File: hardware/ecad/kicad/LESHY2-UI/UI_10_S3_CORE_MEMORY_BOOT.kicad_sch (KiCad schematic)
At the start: 0 parts

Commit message: Complete H2.2.2 S3 core schematic
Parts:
- added C1: Murata GRM1555C1H390JA01D, Capacitor_SMD:C_0402_1005Metric, symbol Leshy2:UI10_S3_DETECTOR_INPUT_CAP
- added C2: KEMET C0402C330J5GACTU, Capacitor_SMD:C_0402_1005Metric, symbol Leshy2:UI10_S3_DETECTOR_OUTPUT_CAP
- added C3: TDK C1005X7R1H104K050BB, Capacitor_SMD:C_0402_1005Metric, symbol Leshy2:UI10_S3_DETECTOR_BYPASS
- added C4: TDK C1005X7R1H104K050BB, Capacitor_SMD:C_0402_1005Metric, symbol Leshy2:UI10_S3_SUPPLY_BYPASS
- added C5: TDK C1608X7R1C105K080AC, Capacitor_SMD:C_0603_1608Metric, symbol Leshy2:UI10_S3_RESET_DELAY_CAP
- added J1: GCT RFPC-SMA32-FN-175-A, Leshy2:RFPC-SMA32-FN-175-A, symbol Leshy2:UI10_S3_EXTERNAL_RP_SMA
- added J2: Hirose U.FL-R-SMT-1(10), Connector_Coaxial:U.FL_Hirose_U.FL-R-SMT-1_Vertical, symbol Leshy2:UI10_S3_RF_BOARD_CONNECTOR
- added J3: Samtec FTSH-105-01-L-DV-K-P-TR, Leshy2:FTSH-105-01-L-DV-K-P-TR, symbol Leshy2:UI10_S3_DBG_HEADER
- added R1: Yageo RC0402FR-0749R9L, Resistor_SMD:R_0402_1005Metric, symbol Leshy2:UI10_S3_RF_COUPLER_TERMINATION
- added R10: Yageo RC0402FR-071KL, Resistor_SMD:R_0402_1005Metric, symbol Leshy2:UI10_S3_DBG_RESET_SERIES
- added R11: Yageo RC0402FR-071KL, Resistor_SMD:R_0402_1005Metric, symbol Leshy2:UI10_S3_DBG_BOOT_SERIES
- added R12: Yageo RC0402FR-07470RL, Resistor_SMD:R_0402_1005Metric, symbol Leshy2:UI10_S3_DBG0_SERIES
- added R13: Yageo RC0402FR-07470RL, Resistor_SMD:R_0402_1005Metric, symbol Leshy2:UI10_S3_DBG1_SERIES
- added R14: Yageo RC0402FR-0710KL, Resistor_SMD:R_0402_1005Metric, symbol Leshy2:UI10_S3_DBG_ID0_STRAP
- added R15: Yageo RC0402FR-0710KL, Resistor_SMD:R_0402_1005Metric, symbol Leshy2:UI10_S3_DBG_ID1_STRAP
- added R16: Yageo RC0402FR-0710KL, Resistor_SMD:R_0402_1005Metric, symbol Leshy2:UI10_S3_BOOT_PULLUP
- added R17: Yageo RC0402FR-0710KL, Resistor_SMD:R_0402_1005Metric, symbol Leshy2:UI10_S3_RESET_PULLUP
- added R2: Yageo RC0402FR-0710KL, Resistor_SMD:R_0402_1005Metric, symbol Leshy2:UI10_S3_DETECTOR_FEEDBACK_RES
- added R3: Yageo RC0402FR-0710KL, Resistor_SMD:R_0402_1005Metric, symbol Leshy2:UI10_S3_DETECTOR_GROUND_RES
- added R4: Panasonic ERJ-2RKF22R0X, Resistor_SMD:R_0402_1005Metric, symbol Leshy2:UI10_PRODUCT_USB_DP_SERIES
- added R5: Panasonic ERJ-2RKF22R0X, Resistor_SMD:R_0402_1005Metric, symbol Leshy2:UI10_PRODUCT_USB_DM_SERIES
- added R6: Yageo RC0402FR-072K2L, Resistor_SMD:R_0402_1005Metric, symbol Leshy2:UI10_SYS_I2C_SCL_PULLUP
- added R7: Yageo RC0402FR-072K2L, Resistor_SMD:R_0402_1005Metric, symbol Leshy2:UI10_SYS_I2C_SDA_PULLUP
- added R8: Yageo RC0402FR-0710KL, Resistor_SMD:R_0402_1005Metric, symbol Leshy2:UI10_SYS_INT_PULLUP
- added R9: Yageo RC0402FR-071KL, Resistor_SMD:R_0402_1005Metric, symbol Leshy2:UI10_S3_DBG_VTREF_SERIES
- added SW1: Alps Alpine SKRTLAE010, Button_Switch_SMD:SW_Push_1P1T-MP_NO_Horizontal_Alps_SKRTLAE010, symbol Leshy2:UI10_S3_RESET_BUTTON
- added SW2: Alps Alpine SKRTLAE010, Button_Switch_SMD:SW_Push_1P1T-MP_NO_Horizontal_Alps_SKRTLAE010, symbol Leshy2:UI10_S3_BOOT_BUTTON
- added U1: ESP32-S3-WROOM-1U-N16R8, RF_Module:ESP32-S3-WROOM-1U, symbol Leshy2:UI10_S3
- added U2: KYOCERA AVX CP0603Q5425ENTR, Leshy2:CP0603Q5425ENTR, symbol Leshy2:UI10_S3_RF_COUPLER
- added U3: Texas Instruments TPD4E05U06DQAR, Package_SON:USON-10_2.5x1.0mm_P0.5mm, symbol Leshy2:UI10_S3_DBG_ESD
- added U4: Murata GRM21BR60J226ME39L, Resistor_SMD:R_0402_1005Metric, symbol Leshy2:UI10_S3_SUPPLY_BULK
- added W1: TE Connectivity 2118651-2, symbol Leshy2:UI10_S3_RF_JUMPER
- added X1: ESP32-S3-WROOM-1U-N16R8 factory U.FL, symbol Leshy2:UI10_S3_FACTORY_ANT
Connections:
- net 3V3_MAIN: now also C4.1 (END_1), R16.1 (END_1), R17.1 (END_1), R6.1 (END_1), R7.1 (END_1), R8.1 (END_1), R9.2 (END_2), U1.2 (3V3), U4.1 (END_1)
- net AON_SAFE_3V3: now also C3.1 (END_1)
- net AUDIO_ARM: now also U1.6 (GPIO6)
- net DISPLAY_SD_SPI_D1: now also U1.4 (GPIO4)
- net I2S_BCLK: now also U1.8 (GPIO15)
- net I2S_DIN: now also R11.2 (END_2), R16.2 (END_2), U1.27 (GPIO0)
- net I2S_DOUT: now also U1.10 (GPIO17)
- net I2S_WS: now also U1.9 (GPIO16)
- net POWER_GROUND: now also C4.2 (END_2), C5.2 (END_2), J3.2 (P2), J3.7 (P7), J3.9 (P9), R14.2 (END_2), R15.2 (END_2), SW1.2 (NO), SW2.2 (NO), U1.1 (GND), U1.40 (GND), U1.41 (EPAD_GND), U4.2 (END_2)
- net S3_DETECT_V: now also C2.1 (END_1), R2.1 (END_1)
- net S3_DETECT_VM: now also R2.2 (END_2), R3.1 (END_1)
- net S3_FORWARD_RF_SAMPLE: now also C1.2 (END_2)
- net S3_RESET_N: now also C5.1 (END_1), R10.2 (END_2), R17.2 (END_2), U1.3 (EN)
- net S3_USB_DM: now also R5.1 (END_1)
- net S3_USB_DP: now also R4.1 (END_1)
- net SAFETY_GROUND: now also C2.2 (END_2), C3.2 (END_2), R3.2 (END_2)
- net SYS_I2C_SCL: now also R6.2 (END_2), U1.38 (GPIO2)
- net SYS_I2C_SDA: now also R7.2 (END_2), U1.39 (GPIO1)
- net SYS_INT_N: now also R8.2 (END_2), U1.26 (GPIO45)
- new net DISPLAY_SD_SPI_D0: U1.16 (GPIO46)
- new net DISPLAY_SD_SPI_SCK: U1.11 (GPIO18)
- new net ENCODER_A: U1.32 (GPIO39)
- new net ENCODER_B: U1.24 (GPIO47)
- new net LCD_BL_PWM: U1.33 (GPIO40)
- new net LCD_CS_N: U1.31 (GPIO38)
- new net LCD_QSPI_D2: U1.34 (GPIO41)
- new net LCD_QSPI_D3: U1.35 (GPIO42)
- new net RP_ALERT_N: U1.15 (GPIO3)
- new net S3_C5_SDIO_CLK: U1.18 (GPIO10)
- new net S3_C5_SDIO_CMD: U1.19 (GPIO11)
- new net S3_C5_SDIO_D0: U1.20 (GPIO12)
- new net S3_C5_SDIO_D1_IRQ: U1.21 (GPIO13)
- new net S3_COUPLER_TERMINATION: R1.1 (END_1), U2.TERM (TERMINATION_50R)
- new net S3_DBG0_CONNECTOR: J3.5 (P5), R12.1 (END_1), U3.4 (D2_PLUS)
- new net S3_DBG1_CONNECTOR: J3.6 (P6), R13.1 (END_1), U3.5 (D2_MINUS)
- new net S3_DBG_BOOT_CONNECTOR_N: J3.4 (P4), R11.1 (END_1), SW2.1 (C1), SW2.3 (C2), U3.2 (D1_MINUS)
- new net S3_DBG_ESD_RETURN: U3.3 (GND_3), U3.8 (GND_8)
- new net S3_DBG_ID0: J3.8 (P8), R14.1 (END_1)
- new net S3_DBG_ID1: J3.10 (P10), R15.1 (END_1)
- new net S3_DBG_RESET_CONNECTOR_N: J3.3 (P3), R10.1 (END_1), SW1.1 (C1), SW1.3 (C2), U3.1 (D1_PLUS)
- new net S3_DBG_VTREF_SENSE: J3.1 (P1), R9.1 (END_1)
- new net S3_EXTERNAL_RF_50R: J1.1 (RF), U2.OUT (RF_OUT)
- new net S3_FORWARD_RF_SAMPLE_RAW: C1.1 (END_1), U2.CPL (COUPLED_FWD)
- new net S3_MODULE_RF_50R: J2.1 (CENTER), U2.IN (RF_IN), W1.A (END_A), W1.B (END_B), X1.1 (FACTORY_UFL)
- new net S3_RF_GROUND: J2.2 (SHELL), R1.2 (END_2)
- new net S3_RP_IPC_CS_N: U1.17 (GPIO9)
- new net S3_RP_IPC_MISO: U1.22 (GPIO14)
- new net S3_RP_IPC_MOSI: U1.23 (GPIO21)
- new net S3_RP_IPC_SCK: U1.25 (GPIO48)
- new net S3_SMA_RF_GROUND: J1.2 (GROUND_TOP_LEFT), J1.3 (GROUND_TOP_RIGHT), J1.4 (GROUND_BOTTOM_LEFT), J1.5 (GROUND_BOTTOM_RIGHT)
- new net S3_UART_SERVICE_RX: R13.2 (END_2), U1.36 (GPIO44)
- new net S3_UART_SERVICE_TX: R12.2 (END_2), U1.37 (GPIO43)
- new net S3_USB_DM_LOCAL: R5.2 (END_2), U1.13 (GPIO19)
- new net S3_USB_DP_LOCAL: R4.2 (END_2), U1.14 (GPIO20)
- new net SD_SPI_CS_N: U1.5 (GPIO5)
- new net UNIT_HOST_SIG0: U1.7 (GPIO7)
- new net UNIT_HOST_SIG1: U1.12 (GPIO8)
- no-connect marks 19 -> 7
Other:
- title: (none) -> Leshy2 — exact S3 core, boot, USB, service and RF feed

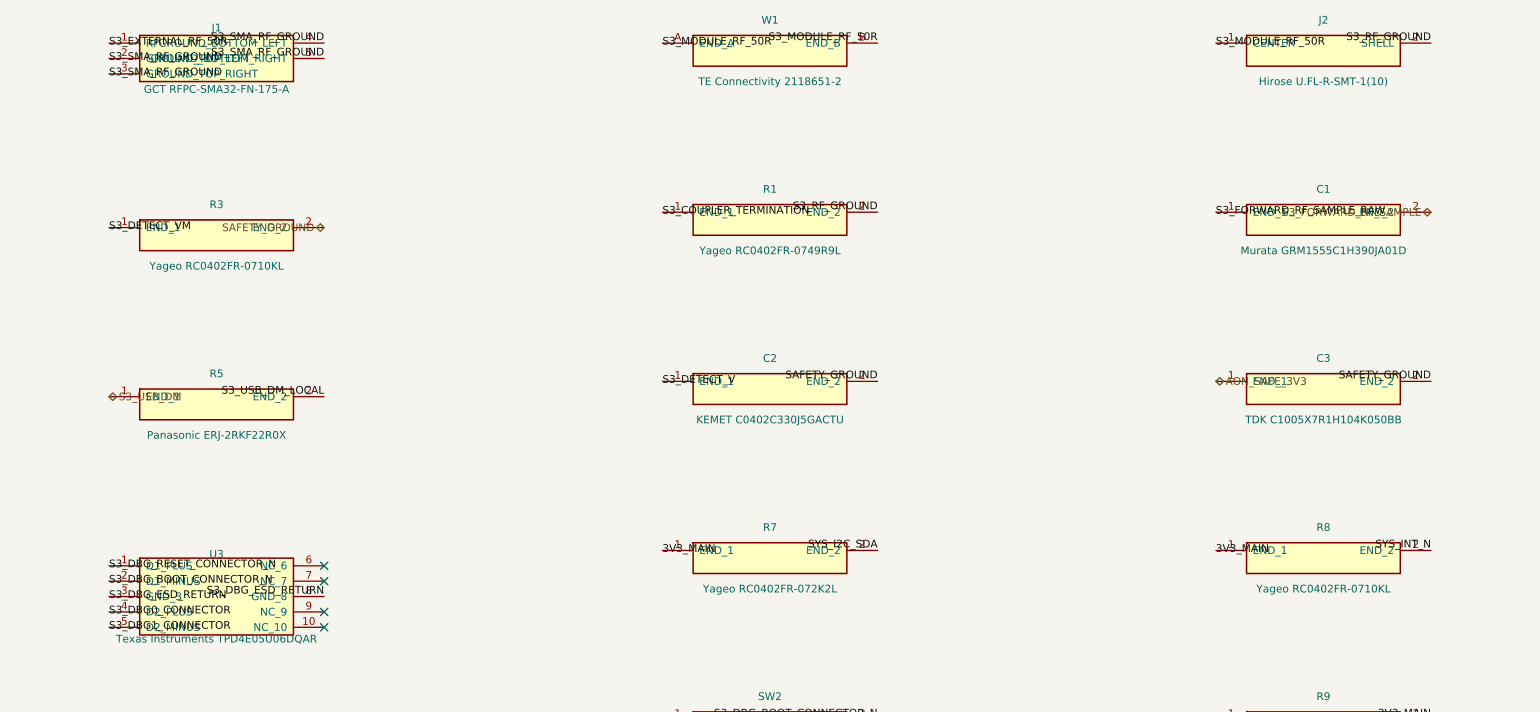
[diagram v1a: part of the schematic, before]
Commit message: complete exact H2.2.7 broadcast receiver schematic
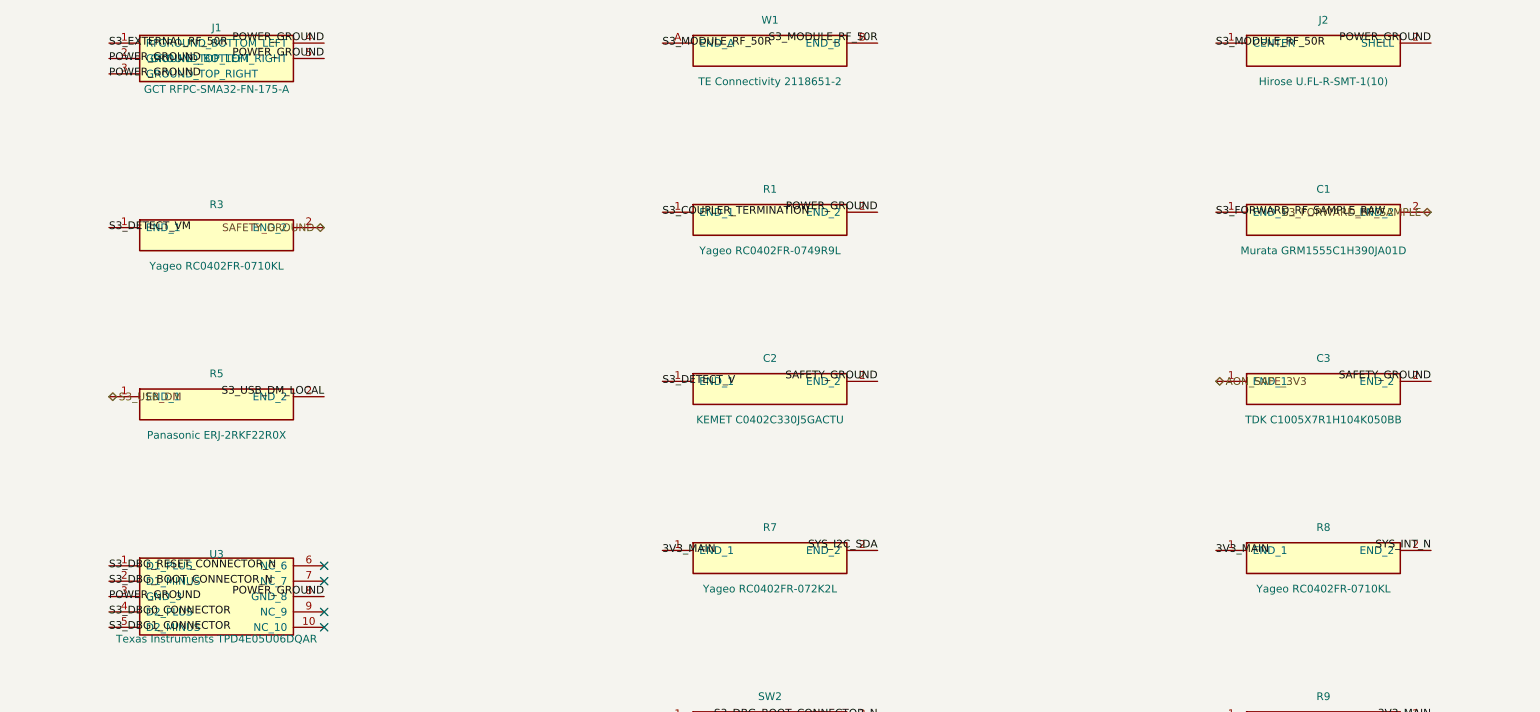
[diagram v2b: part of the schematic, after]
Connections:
- net S3_DBG_ESD_RETURN is gone; now on net POWER_GROUND: U3.3 (GND_3), U3.8 (GND_8)
- net S3_RF_GROUND is gone; now on net POWER_GROUND: J2.2 (SHELL), R1.2 (END_2)
- net S3_SMA_RF_GROUND is gone; now on net POWER_GROUND: J1.2 (GROUND_TOP_LEFT), J1.3 (GROUND_TOP_RIGHT), J1.4 (GROUND_BOTTOM_LEFT), J1.5 (GROUND_BOTTOM_RIGHT)
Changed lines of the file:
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@@
+	)
+	(label "POWER_GROUND"
+		(at 134.62 50.80 0)
+		(effects (font (size 1.27 1.27)))
+	)
+	(label "POWER_GROUND"
+		(at 134.62 53.34 0)
+		(effects (font (size 1.27 1.27)))
+	)
+	(label "POWER_GROUND"
+		(at 170.18 48.26 180)
+		(effects (font (size 1.27 1.27)) (justify right bottom))
+	)
+	(label "POWER_GROUND"
+		(at 170.18 50.80 180)
+		(effects (font (size 1.27 1.27)) (justify right bottom))
+	)
+	(label "POWER_GROUND"
+		(at 353.06 48.26 180)
+		(effects (font (size 1.27 1.27)) (justify right bottom))
+	)
+	(label "POWER_GROUND"
+		(at 261.62 76.20 180)
+		(effects (font (size 1.27 1.27)) (justify right bottom))
 	)
 	(label "POWER_GROUND"
@@
 	(label "POWER_GROUND"
 		(at 444.50 139.70 180)
+		(effects (font (size 1.27 1.27)) (justify right bottom))
+	)
+	(label "POWER_GROUND"
+		(at 134.62 139.70 0)
+		(effects (font (size 1.27 1.27)))
+	)
+	(label "POWER_GROUND"
+		(at 170.18 139.70 180)
 		(effects (font (size 1.27 1.27)) (justify right bottom))
 	)
@@
 		(effects (font (size 1.27 1.27)))
 	)
-	(label "S3_DBG_ESD_RETURN"
-		(at 134.62 139.70 0)
-		(effects (font (size 1.27 1.27)))
-	)
-	(label "S3_DBG_ESD_RETURN"
-		(at 170.18 139.70 180)
-		(effects (font (size 1.27 1.27)) (justify right bottom))
-	)
 	(label "S3_DBG_ID0"
 		(at 444.50 137.16 180)
@@
 		(effects (font (size 1.27 1.27)) (justify right bottom))
 	)
-	(label "S3_RF_GROUND"
-		(at 353.06 48.26 180)
-		(effects (font (size 1.27 1.27)) (justify right bottom))
-	)
-	(label "S3_RF_GROUND"
-		(at 261.62 76.20 180)
-		(effects (font (size 1.27 1.27)) (justify right bottom))
-	)
 	(hierarchical_label "S3_RP_IPC_CS_N"
 		(shape bidirectional)
@@
 		(effects (font (size 1.27 1.27)) (justify right bottom))
 	)
-	(label "S3_SMA_RF_GROUND"
-		(at 134.62 50.80 0)
-		(effects (font (size 1.27 1.27)))
-	)
-	(label "S3_SMA_RF_GROUND"
-		(at 134.62 53.34 0)
-		(effects (font (size 1.27 1.27)))
-	)
-	(label "S3_SMA_RF_GROUND"
-		(at 170.18 48.26 180)
-		(effects (font (size 1.27 1.27)) (justify right bottom))
-	)
-	(label "S3_SMA_RF_GROUND"
-		(at 170.18 50.80 180)
-		(effects (font (size 1.27 1.27)) (justify right bottom))
-	)

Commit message: complete H2 schematic review package
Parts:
- renumbered C1 to C10001, C2 to C10002, C3 to C10003, C4 to C10004, C5 to C10005, J1 to J10001, J2 to J10002, J3 to J10003, R1 to R10001, R2 to R10002, R3 to R10003, R4 to R10004, R5 to R10005, R6 to R10006, R7 to R10007, R8 to R10008, R9 to R10009, R10 to R10010, R11 to R10011, R12 to R10012, R13 to R10013, R14 to R10014, R15 to R10015, R16 to R10016, R17 to R10017, SW1 to SW10001, SW2 to SW10002, U1 to U10001, U2 to U10002, U3 to U10003, U4 to U10004, W1 to W10001, X1 to X10001
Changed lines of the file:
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@@
 		(on_board yes)
 		(dnp no)
-		(property "Reference" "U1"
+		(property "Reference" "U10001"
 			(at 60.96 47.50 0)
 			(show_name no)
@@
 			(project "LESHY2-UI"
 				(path "/209011ee-f1df-5077-bb46-849d9306b52f"
-					(reference "U1")
+					(reference "U10001")
 					(unit 1)
 				)
@@
 		(on_board yes)
 		(dnp no)
-		(property "Reference" "J1"
+		(property "Reference" "J10001"
 			(at 152.40 45.72 0)
 			(show_name no)
@@
 			(project "LESHY2-UI"
 				(path "/209011ee-f1df-5077-bb46-849d9306b52f"
-					(reference "J1")
+					(reference "J10001")
 					(unit 1)
 				)
@@
 		(on_board no)
 		(dnp no)
-		(property "Reference" "W1"
+		(property "Reference" "W10001"
 			(at 243.84 44.45 0)
 			(show_name no)
@@
 			(project "LESHY2-UI"
 				(path "/209011ee-f1df-5077-bb46-849d9306b52f"
-					(reference "W1")
+					(reference "W10001")
 					(unit 1)
 				)
@@
 		(on_board yes)
 		(dnp no)
-		(property "Reference" "J2"
+		(property "Reference" "J10002"
 			(at 335.28 44.45 0)
 			(show_name no)
@@
 			(project "LESHY2-UI"
 				(path "/209011ee-f1df-5077-bb46-849d9306b52f"
-					(reference "J2")
+					(reference "J10002")
 					(unit 1)
 				)
@@
 		(on_board yes)
 		(dnp no)
-		(property "Reference" "U2"
+		(property "Reference" "U10002"
 			(at 426.72 44.45 0)
 			(show_name no)
@@
 			(project "LESHY2-UI"
 				(path "/209011ee-f1df-5077-bb46-849d9306b52f"
-					(reference "U2")
+					(reference "U10002")
 					(unit 1)
 				)
@@
 		(on_board yes)
 		(dnp no)
-		(property "Reference" "R1"
+		(property "Reference" "R10001"
 			(at 243.84 72.39 0)
 			(show_name no)
@@
 			(project "LESHY2-UI"
 				(path "/209011ee-f1df-5077-bb46-849d9306b52f"
-					(reference "R1")
+					(reference "R10001")
 					(unit 1)
 				)
@@
 		(on_board yes)
 		(dnp no)
-		(property "Reference" "C1"
+		(property "Reference" "C10001"
 			(at 335.28 72.39 0)
 			(show_name no)
@@
 			(project "LESHY2-UI"
 				(path "/209011ee-f1df-5077-bb46-849d9306b52f"
-					(reference "C1")
+					(reference "C10001")
 					(unit 1)
 				)
@@
 		(on_board yes)
 		(dnp no)
-		(property "Reference" "R2"
+		(property "Reference" "R10002"
 			(at 426.72 72.39 0)
 			(show_name no)
@@
 			(project "LESHY2-UI"
 				(path "/209011ee-f1df-5077-bb46-849d9306b52f"
-					(reference "R2")
+					(reference "R10002")
 					(unit 1)
 				)
@@
 		(on_board yes)
 		(dnp no)
-		(property "Reference" "R3"
+		(property "Reference" "R10003"
 			(at 152.40 74.93 0)
 			(show_name no)
@@
 			(project "LESHY2-UI"
 				(path "/209011ee-f1df-5077-bb46-849d9306b52f"
-					(reference "R3")
+					(reference "R10003")
 					(unit 1)
 				)
@@
 		(on_board yes)
 		(dnp no)
-		(property "Reference" "C2"
+		(property "Reference" "C10002"
 			(at 243.84 100.33 0)
 			(show_name no)
@@
 			(project "LESHY2-UI"
 				(path "/209011ee-f1df-5077-bb46-849d9306b52f"
-					(reference "C2")
+					(reference "C10002")
 					(unit 1)
 				)
@@
 		(on_board yes)
 		(dnp no)
-		(property "Reference" "C3"
+		(property "Reference" "C10003"
 			(at 335.28 100.33 0)
 			(show_name no)
@@
 			(project "LESHY2-UI"
 				(path "/209011ee-f1df-5077-bb46-849d9306b52f"
-					(reference "C3")
+					(reference "C10003")
 					(unit 1)
 				)
@@
 		(on_board yes)
 		(dnp no)
-		(property "Reference" "R4"
+		(property "Reference" "R10004"
 			(at 426.72 100.33 0)
 			(show_name no)
@@
 			(project "LESHY2-UI"
 				(path "/209011ee-f1df-5077-bb46-849d9306b52f"
-					(reference "R4")
+					(reference "R10004")
 					(unit 1)
 				)
@@
 		(on_board yes)
 		(dnp no)
-		(property "Reference" "R5"
+		(property "Reference" "R10005"
 			(at 152.40 102.87 0)
 			(show_name no)
@@
 			(project "LESHY2-UI"
 				(path "/209011ee-f1df-5077-bb46-849d9306b52f"
-					(reference "R5")
+					(reference "R10005")
 					(unit 1)
 				)
@@
 		(on_board yes)
 		(dnp no)
-		(property "Reference" "R6"
+		(property "Reference" "R10006"
 			(at 60.96 123.19 0)
 			(show_name no)
@@
 			(project "LESHY2-UI"
 				(path "/209011ee-f1df-5077-bb46-849d9306b52f"
-					(reference "R6")
+					(reference "R10006")
 					(unit 1)
 				)
@@
 		(on_board yes)
 		(dnp no)
-		(property "Reference" "R7"
+		(property "Reference" "R10007"
 			(at 243.84 128.27 0)
 			(show_name no)
@@
 			(project "LESHY2-UI"
 				(path "/209011ee-f1df-5077-bb46-849d9306b52f"
-					(reference "R7")
+					(reference "R10007")
 					(unit 1)
 				)
@@
 		(on_board yes)
 		(dnp no)
-		(property "Reference" "R8"
+		(property "Reference" "R10008"
 			(at 335.28 128.27 0)
 			(show_name no)
@@
 			(project "LESHY2-UI"
 				(path "/209011ee-f1df-5077-bb46-849d9306b52f"
-					(reference "R8")
+					(reference "R10008")
 					(unit 1)
 				)
@@
 		(on_board yes)
 		(dnp no)
-		(property "Reference" "J3"
+		(property "Reference" "J10003"
 			(at 426.72 130.16 0)
 			(show_name no)
@@
 			(project "LESHY2-UI"
 				(path "/209011ee-f1df-5077-bb46-849d9306b52f"
-					(reference "J3")
+					(reference "J10003")
 					(unit 1)
 				)
@@
 		(on_board yes)
 		(dnp no)
-		(property "Reference" "U3"
+		(property "Reference" "U10003"
 			(at 152.40 132.70 0)
 			(show_name no)
@@
 			(project "LESHY2-UI"
 				(path "/209011ee-f1df-5077-bb46-849d9306b52f"
-					(reference "U3")
+					(reference "U10003")
 					(unit 1)
 				)
@@
 		(on_board yes)
 		(dnp no)
-		(property "Reference" "SW1"
+		(property "Reference" "SW10001"
 			(at 60.96 151.13 0)
 			(show_name no)
@@
 			(project "LESHY2-UI"
 				(path "/209011ee-f1df-5077-bb46-849d9306b52f"
-					(reference "SW1")
+					(reference "SW10001")
 					(unit 1)
 				)
@@
 		(on_board yes)
 		(dnp no)
-		(property "Reference" "SW2"
+		(property "Reference" "SW10002"
 			(at 243.84 156.21 0)
 			(show_name no)
@@
 			(project "LESHY2-UI"
 				(path "/209011ee-f1df-5077-bb46-849d9306b52f"
-					(reference "SW2")
+					(reference "SW10002")
 					(unit 1)
 				)
@@
 		(on_board yes)
 		(dnp no)
-		(property "Reference" "R9"
+		(property "Reference" "R10009"
 			(at 335.28 156.21 0)
 			(show_name no)
@@
 			(project "LESHY2-UI"
 				(path "/209011ee-f1df-5077-bb46-849d9306b52f"
-					(reference "R9")
+					(reference "R10009")
 					(unit 1)
 				)
@@
 		(on_board yes)
 		(dnp no)
-		(property "Reference" "R10"
+		(property "Reference" "R10010"
 			(at 426.72 163.83 0)
 			(show_name no)
@@
 			(project "LESHY2-UI"
 				(path "/209011ee-f1df-5077-bb46-849d9306b52f"
-					(reference "R10")
+					(reference "R10010")
 					(unit 1)
 				)
@@
 		(on_board yes)
 		(dnp no)
-		(property "Reference" "R11"
+		(property "Reference" "R10011"
 			(at 152.40 166.37 0)
 			(show_name no)
@@
 			(project "LESHY2-UI"
 				(path "/209011ee-f1df-5077-bb46-849d9306b52f"
-					(reference "R11")
+					(reference "R10011")
 					(unit 1)
 				)
@@
 		(on_board yes)
 		(dnp no)
-		(property "Reference" "R12"
+		(property "Reference" "R10012"
 			(at 60.96 179.07 0)
 			(show_name no)
@@
 			(project "LESHY2-UI"
 				(path "/209011ee-f1df-5077-bb46-849d9306b52f"
-					(reference "R12")
+					(reference "R10012")
 					(unit 1)
 				)
@@
 		(on_board yes)
 		(dnp no)
-		(property "Reference" "R13"
+		(property "Reference" "R10013"
 			(at 243.84 184.15 0)
 			(show_name no)
@@
 			(project "LESHY2-UI"
 				(path "/209011ee-f1df-5077-bb46-849d9306b52f"
-					(reference "R13")
+					(reference "R10013")
 					(unit 1)
 				)
@@
 		(on_board yes)
 		(dnp no)
-		(property "Reference" "R14"
+		(property "Reference" "R10014"
 			(at 335.28 184.15 0)
 			(show_name no)
@@
 			(project "LESHY2-UI"
 				(path "/209011ee-f1df-5077-bb46-849d9306b52f"
-					(reference "R14")
+					(reference "R10014")
 					(unit 1)
 				)
@@
 		(on_board yes)
 		(dnp no)
-		(property "Reference" "R15"
+		(property "Reference" "R10015"
 			(at 426.72 191.77 0)
 			(show_name no)
@@
 			(project "LESHY2-UI"
 				(path "/209011ee-f1df-5077-bb46-849d9306b52f"
-					(reference "R15")
+					(reference "R10015")
 					(unit 1)
 				)
@@
 		(on_board yes)
 		(dnp no)
-		(property "Reference" "R16"
+		(property "Reference" "R10016"
 			(at 152.40 194.31 0)
 			(show_name no)
@@
 			(project "LESHY2-UI"
 				(path "/209011ee-f1df-5077-bb46-849d9306b52f"
-					(reference "R16")
+					(reference "R10016")
 					(unit 1)
 				)
@@
 		(on_board yes)
 		(dnp no)
-		(property "Reference" "U4"
+		(property "Reference" "U10004"
 			(at 60.96 207.01 0)
 			(show_name no)
@@
 			(project "LESHY2-UI"
 				(path "/209011ee-f1df-5077-bb46-849d9306b52f"
-					(reference "U4")
+					(reference "U10004")
 					(unit 1)
 				)
@@
 		(on_board yes)
 		(dnp no)
-		(property "Reference" "C4"
+		(property "Reference" "C10004"
 			(at 243.84 212.09 0)
 			(show_name no)
@@
 			(project "LESHY2-UI"
 				(path "/209011ee-f1df-5077-bb46-849d9306b52f"
-					(reference "C4")
+					(reference "C10004")
 					(unit 1)
 				)
@@
 		(on_board yes)
 		(dnp no)
-		(property "Reference" "C5"
+		(property "Reference" "C10005"
 			(at 335.28 212.09 0)
 			(show_name no)
@@
 			(project "LESHY2-UI"
 				(path "/209011ee-f1df-5077-bb46-849d9306b52f"
-					(reference "C5")
+					(reference "C10005")
 					(unit 1)
 				)
@@
 		(on_board yes)
 		(dnp no)
-		(property "Reference" "R17"
+		(property "Reference" "R10017"
 			(at 426.72 219.71 0)
 			(show_name no)
@@
 			(project "LESHY2-UI"
 				(path "/209011ee-f1df-5077-bb46-849d9306b52f"
-					(reference "R17")
+					(reference "R10017")
 					(unit 1)
 				)
@@
 		(on_board no)
 		(dnp no)
-		(property "Reference" "X1"
+		(property "Reference" "X10001"
 			(at 152.40 222.25 0)
 			(show_name no)
@@
 			(project "LESHY2-UI"
 				(path "/209011ee-f1df-5077-bb46-849d9306b52f"
-					(reference "X1")
-					(unit 1)
-				)
+					(reference "X10001")
+					(unit 1)
+				)
